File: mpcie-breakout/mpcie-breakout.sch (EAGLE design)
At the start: 36 parts, among them K1 694108106102, U1 IP4234CZ6, U2 LD1085D2T33R, X1 MPCIE-JAE, X2 MINI-USB-SHIELD-UX60-MB-5ST

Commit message: mpcie-breakout: Fix R4 (0603, not 0201 part)
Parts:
- R4: DESCRIPTION RES SMD 1M OHM 5% 1/20W 0201 -> RES SMD 1M OHM 5% 1/10W 0603; LINK http://www.digikey.com/product-detail/en/samsung-electro-me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 -> http://www.digikey.com/product-detail/en/yageo/RC0603JR-071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; MANUFACTURER Samsung Electro-Mechanics America, Inc. -> Yageo; MANUFACTURERPARTNUMBER RC0603J105CS -> RC0603JR-071ML; SOURCEPARTNUMBER 1276-3856-1-ND -> 311-1.0MGRCT-ND
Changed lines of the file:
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@@
 <part name="R4" library="rc-sysmocom" deviceset="RESISTOR" device="_0603" value="1M">
 <attribute name="CLASS" value="RESISTOR"/>
-<attribute name="DESCRIPTION" value="RES SMD 1M OHM 5% 1/20W 0201"/>
-<attribute name="LINK" value="http://www.digikey.com/product-detail/en/samsung-electro-mechanics-america-inc/RC0603J105CS/1276-3856-1-ND/3966828"/>
-<attribute name="MANUFACTURER" value="Samsung Electro-Mechanics America, Inc."/>
-<attribute name="MANUFACTURERPARTNUMBER" value="RC0603J105CS"/>
+<attribute name="DESCRIPTION" value="RES SMD 1M OHM 5% 1/10W 0603"/>
+<attribute name="LINK" value="http://www.digikey.com/product-detail/en/yageo/RC0603JR-071ML/311-1.0MGRCT-ND/729625"/>
+<attribute name="MANUFACTURER" value="Yageo"/>
+<attribute name="MANUFACTURERPARTNUMBER" value="RC0603JR-071ML"/>
 <attribute name="POPULATED" value="TRUE"/>
 <attribute name="ROHSCERTIFICATE" value="UNKNOWN ROHS CERTIFICATE"/>
 <attribute name="SOURCE" value="DIGIKEY"/>
-<attribute name="SOURCEPARTNUMBER" value="1276-3856-1-ND"/>
+<attribute name="SOURCEPARTNUMBER" value="311-1.0MGRCT-ND"/>
 </part>
 <part name="C9" library="rc-sysmocom" deviceset="CAP_CERAMIC" device="_0603" value="100n">
@@
 <instance part="GND11" gate="1" x="30.48" y="96.52"/>
 <instance part="R4" gate="G$1" x="236.22" y="50.8" rot="R90">
+<attribute name="LINK" x="236.22" y="50.8" size="1.778" layer="96" display="off"/>
 <attribute name="DESCRIPTION" x="236.22" y="50.8" size="1.778" layer="96" display="off"/>
 <attribute name="MANUFACTURER" x="236.22" y="50.8" size="1.778" layer="96" display="off"/>
@@
 <attribute name="POPULATED" x="236.22" y="50.8" size="1.778" layer="96" display="off"/>
 <attribute name="CLASS" x="236.22" y="50.8" size="1.778" layer="96" display="off"/>
-<attribute name="LINK" x="236.22" y="50.8" size="1.778" layer="96" display="off"/>
 </instance>
 <instance part="C9" gate="G$1" x="228.6" y="50.8" smashed="yes" rot="R90">

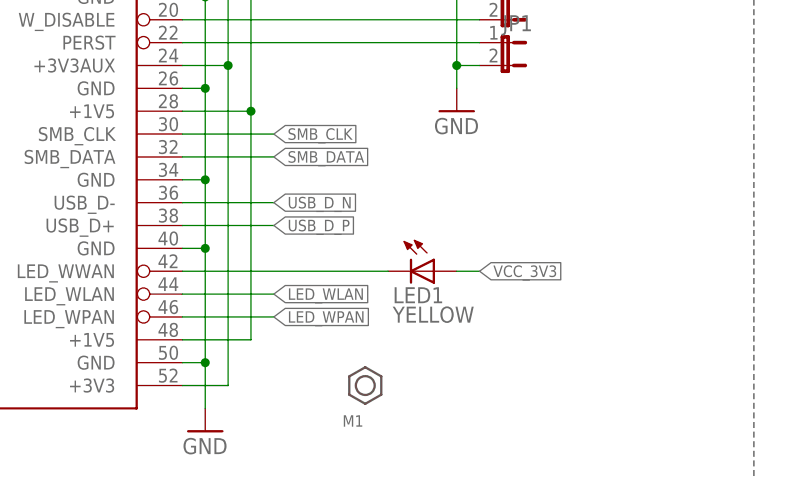
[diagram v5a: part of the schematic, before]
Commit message: mpcie-breakout: Add series LED for LED_WWAN
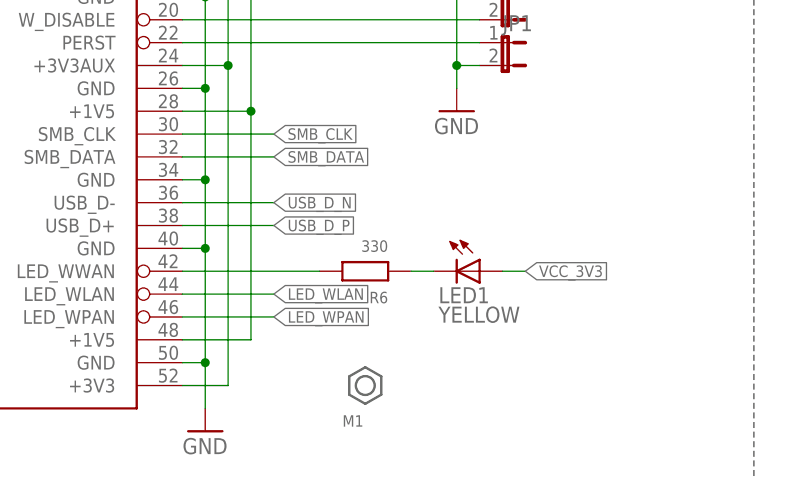
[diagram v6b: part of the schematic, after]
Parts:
- added R6: 330, rc-sysmocom:RESISTOR_0603
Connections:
- new net N$2: LED1.C, R6.1
- net N$3: now also R6.2; no longer LED1.C
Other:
- moved on the sheet: LED1
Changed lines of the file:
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@@
 <schematic xreflabel="%F%N/%S.%C%R" xrefpart="/%S.%C%R">
 <attributes>
-<attribute name="VERSION" value="v1"/>
+<attribute name="VERSION" value="v2"/>
 </attributes>
 <variantdefs>
@@
 <attribute name="SOURCE" value="DIGIKEY"/>
 <attribute name="SOURCEPARTNUMBER" value="490-7217-1-ND"/>
+</part>
+<part name="R6" library="rc-sysmocom" deviceset="RESISTOR" device="_0603" value="330">
+<attribute name="CLASS" value="RESISTOR"/>
+<attribute name="DESCRIPTION" value="RES SMD 330 OHM 5% 1/10W 0603"/>
+<attribute name="LINK" value="http://www.digikey.com/product-detail/en/yageo/RC0603JR-07330RL/311-330GRCT-ND/729716"/>
+<attribute name="MANUFACTURER" value="Yageo"/>
+<attribute name="MANUFACTURERPARTNUMBER" value="RC0603JR-07330RL"/>
+<attribute name="POPULATED" value="TRUE"/>
+<attribute name="ROHSCERTIFICATE" value="UNKNOWN ROHS CERTIFICATE"/>
+<attribute name="SOURCE" value="DIGIKEY"/>
+<attribute name="SOURCEPARTNUMBER" value="311-330GRCT-ND"/>
 </part>
 </parts>
@@
 <attribute name="LINK" x="55.88" y="106.68" size="1.778" layer="96" display="off"/>
 </instance>
-<instance part="LED1" gate="G$1" x="93.98" y="22.86" rot="R270">
-<attribute name="DESCRIPTION" x="93.98" y="22.86" size="1.778" layer="96" display="off"/>
-<attribute name="MANUFACTURER" x="93.98" y="22.86" size="1.778" layer="96" display="off"/>
-<attribute name="MANUFACTURERPARTNUMBER" x="93.98" y="22.86" size="1.778" layer="96" display="off"/>
-<attribute name="SOURCE" x="93.98" y="22.86" size="1.778" layer="96" display="off"/>
-<attribute name="SOURCEPARTNUMBER" x="93.98" y="22.86" size="1.778" layer="96" display="off"/>
-<attribute name="ROHSCERTIFICATE" x="93.98" y="22.86" size="1.778" layer="96" display="off"/>
-<attribute name="POPULATED" x="93.98" y="22.86" size="1.778" layer="96" display="off"/>
-<attribute name="CLASS" x="93.98" y="22.86" size="1.778" layer="96" display="off"/>
-<attribute name="LINK" x="93.98" y="22.86" size="1.778" layer="96" display="off"/>
+<instance part="LED1" gate="G$1" x="99.06" y="22.86" rot="R270">
+<attribute name="DESCRIPTION" x="99.06" y="22.86" size="1.778" layer="96" display="off"/>
+<attribute name="MANUFACTURER" x="99.06" y="22.86" size="1.778" layer="96" display="off"/>
+<attribute name="MANUFACTURERPARTNUMBER" x="99.06" y="22.86" size="1.778" layer="96" display="off"/>
+<attribute name="SOURCE" x="99.06" y="22.86" size="1.778" layer="96" display="off"/>
+<attribute name="SOURCEPARTNUMBER" x="99.06" y="22.86" size="1.778" layer="96" display="off"/>
+<attribute name="ROHSCERTIFICATE" x="99.06" y="22.86" size="1.778" layer="96" display="off"/>
+<attribute name="POPULATED" x="99.06" y="22.86" size="1.778" layer="96" display="off"/>
+<attribute name="CLASS" x="99.06" y="22.86" size="1.778" layer="96" display="off"/>
+<attribute name="LINK" x="99.06" y="22.86" size="1.778" layer="96" display="off"/>
 </instance>
 <instance part="JP1" gate="A" x="101.6" y="48.26" rot="R270">
@@
 <attribute name="POPULATED" x="185.42" y="114.3" size="1.778" layer="96" display="off"/>
 <attribute name="CLASS" x="185.42" y="114.3" size="1.778" layer="96" display="off"/>
+</instance>
+<instance part="R6" gate="G$1" x="86.36" y="22.86" rot="R180">
+<attribute name="DESCRIPTION" x="86.36" y="22.86" size="1.778" layer="96" rot="R90" display="off"/>
+<attribute name="MANUFACTURER" x="86.36" y="22.86" size="1.778" layer="96" rot="R90" display="off"/>
+<attribute name="MANUFACTURERPARTNUMBER" x="86.36" y="22.86" size="1.778" layer="96" rot="R90" display="off"/>
+<attribute name="SOURCE" x="86.36" y="22.86" size="1.778" layer="96" rot="R90" display="off"/>
+<attribute name="SOURCEPARTNUMBER" x="86.36" y="22.86" size="1.778" layer="96" rot="R90" display="off"/>
+<attribute name="ROHSCERTIFICATE" x="86.36" y="22.86" size="1.778" layer="96" rot="R90" display="off"/>
+<attribute name="POPULATED" x="86.36" y="22.86" size="1.778" layer="96" rot="R90" display="off"/>
+<attribute name="CLASS" x="86.36" y="22.86" size="1.778" layer="96" rot="R90" display="off"/>
+<attribute name="LINK" x="86.36" y="22.86" size="1.778" layer="96" rot="R90" display="off"/>
 </instance>
 </instances>
@@
 <segment>
 <pinref part="LED1" gate="G$1" pin="A"/>
-<wire x1="96.52" y1="22.86" x2="99.06" y2="22.86" width="0.1524" layer="91"/>
-<label x="99.06" y="22.86" size="1.27" layer="95" xref="yes"/>
+<wire x1="101.6" y1="22.86" x2="104.14" y2="22.86" width="0.1524" layer="91"/>
+<label x="104.14" y="22.86" size="1.27" layer="95" xref="yes"/>
 </segment>
 <segment>
@@
 <segment>
 <pinref part="X1" gate="G$1" pin="LED_WWAN"/>
-<wire x1="66.04" y1="22.86" x2="88.9" y2="22.86" width="0.1524" layer="91"/>
-<pinref part="LED1" gate="G$1" pin="C"/>
+<wire x1="66.04" y1="22.86" x2="81.28" y2="22.86" width="0.1524" layer="91"/>
+<pinref part="R6" gate="G$1" pin="2"/>
 </segment>
 </net>
@@
 </segment>
 </net>
+<net name="N$2" class="0">
+<segment>
+<pinref part="LED1" gate="G$1" pin="C"/>
+<pinref part="R6" gate="G$1" pin="1"/>
+<wire x1="91.44" y1="22.86" x2="93.98" y2="22.86" width="0.1524" layer="91"/>
+</segment>
+</net>

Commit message: mpcie-breakout: mark C4  as POPULATED=FALSE
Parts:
- C4: POPULATED TRUE -> FALSE
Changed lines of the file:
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@@
 <attribute name="MANUFACTURER" value="UNKNOWN MANUFACTURER"/>
 <attribute name="MANUFACTURERPARTNUMBER" value="UNKNOWN MANUFACTURER PART NUMBER"/>
-<attribute name="POPULATED" value="TRUE"/>
+<attribute name="POPULATED" value="FALSE"/>
 <attribute name="ROHSCERTIFICATE" value="UNKNOWN ROHS CERTIFICATE"/>
 <attribute name="SOURCE" value="UNKNOWN SOURCE"/>

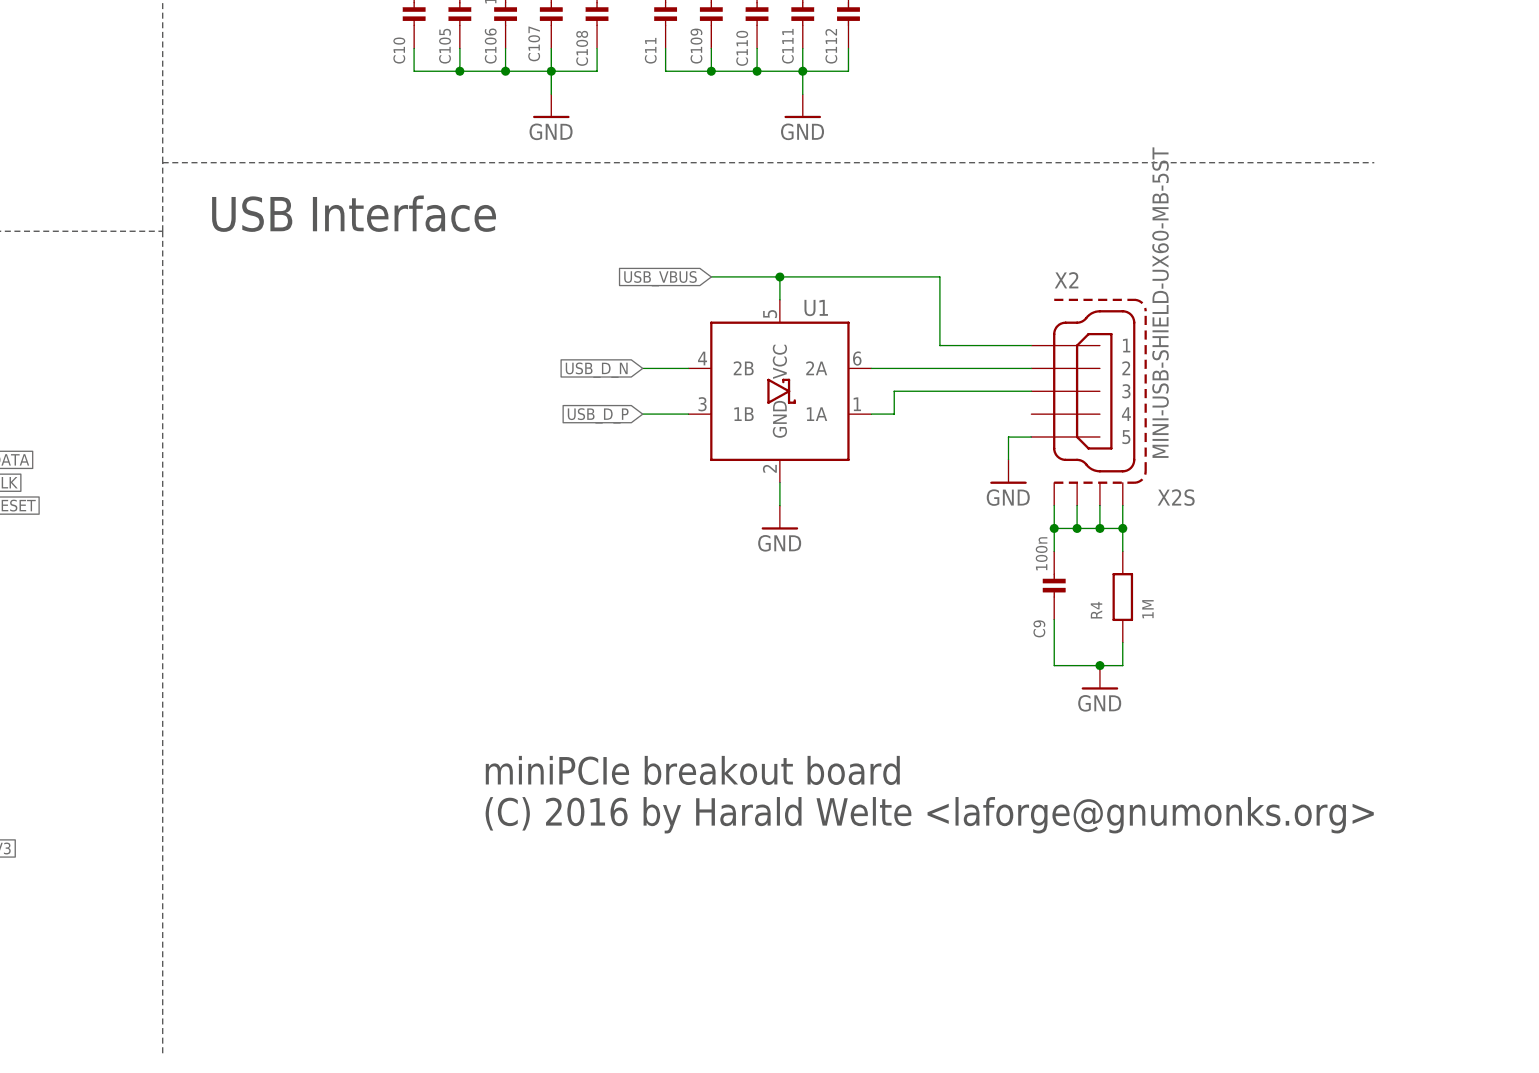
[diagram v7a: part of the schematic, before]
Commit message: mpcie-breakout: Enlarge to 70x70mm, add SMA, U.FL and Mounting Holes
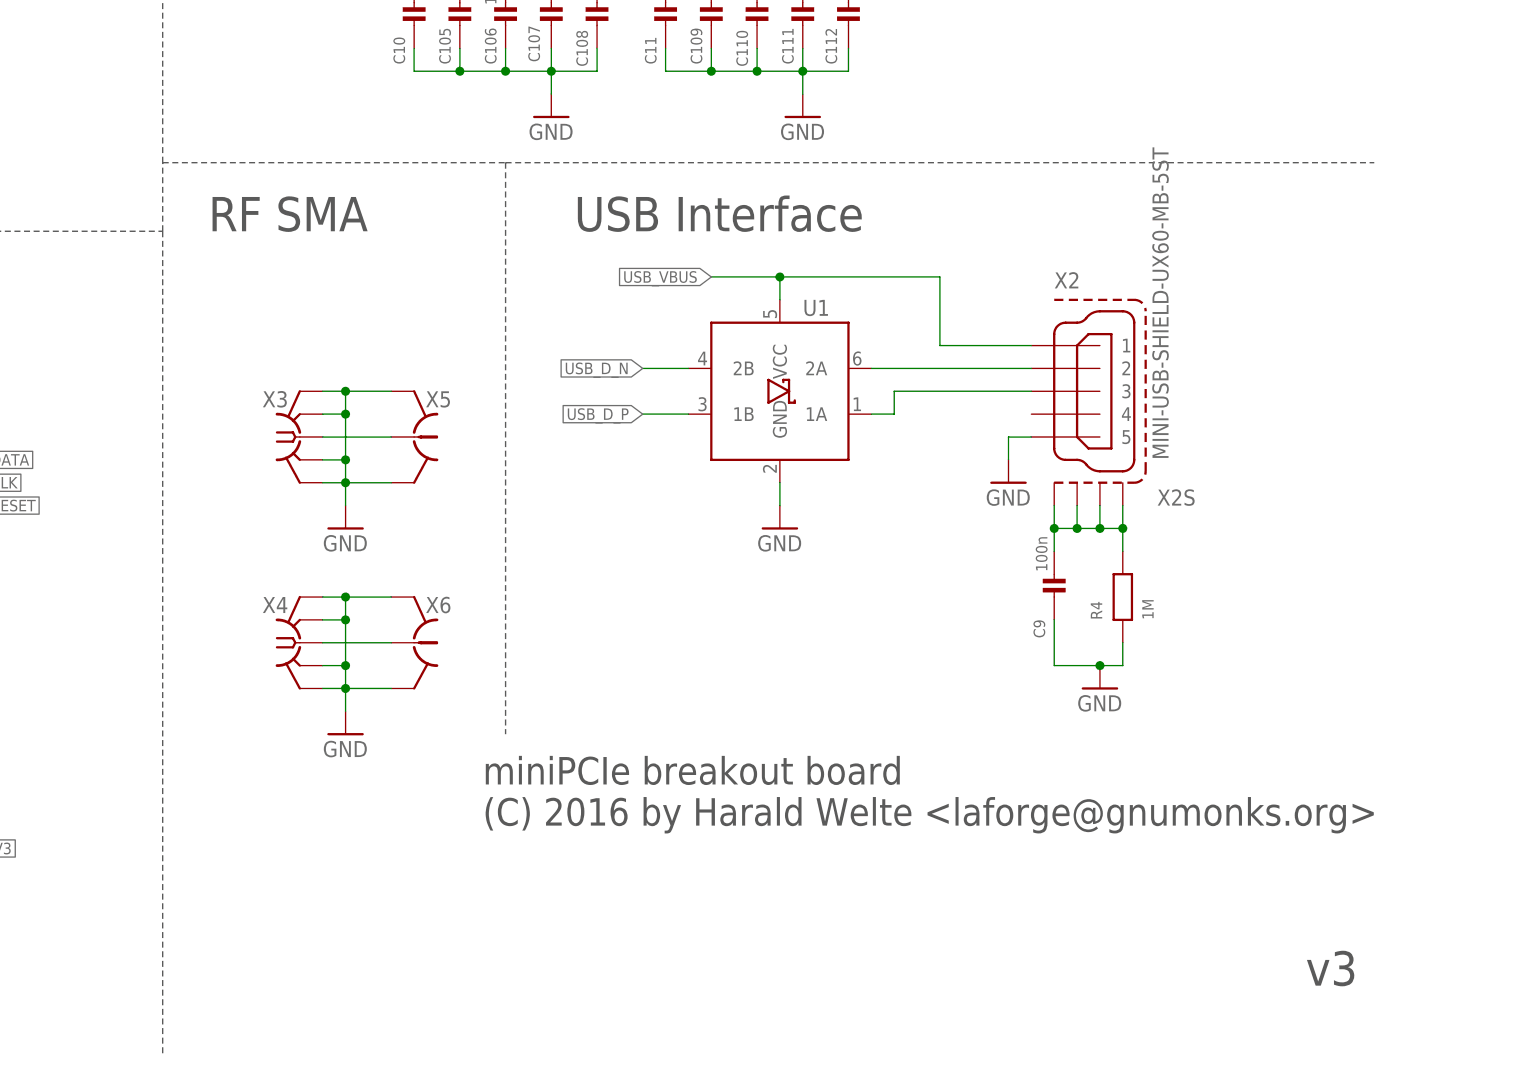
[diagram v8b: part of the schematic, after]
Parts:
- added X3, X4: (no value), laforge:SMA-F-S-TH
- added X5, X6: (no value), laforge:HRS_UFL
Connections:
- new net N$13: X3.1, X5.1
- new net N$14: X4.1, X6.1
- net GND: now also X3.GND@1, X3.GND@2, X3.GND@3, X3.GND@4, X4.GND@1, X4.GND@2, X4.GND@3, X4.GND@4, X5.GND@1, X5.GND@2, X6.GND@1, X6.GND@2
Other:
- note added: "RF SMA"
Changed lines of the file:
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@@
 <schematic xreflabel="%F%N/%S.%C%R" xrefpart="/%S.%C%R">
 <attributes>
-<attribute name="VERSION" value="v2"/>
+<attribute name="VERSION" value="v3"/>
 </attributes>
 <variantdefs>
@@
 </class>
 <class number="1" name="usb" width="0.5" drill="0.15">
+</class>
+<class number="2" name="50 ohm" width="0.9" drill="0">
+<clearance class="2" value="0.152"/>
 </class>
 <class number="3" name="supply" width="0.6" drill="0">
@@
 <attribute name="SOURCEPARTNUMBER" value="311-330GRCT-ND"/>
 </part>
+<part name="X3" library="laforge" deviceset="SMA-F" device="-S-TH"/>
+<part name="X4" library="laforge" deviceset="SMA-F" device="-S-TH"/>
+<part name="X5" library="laforge" deviceset="HRS_UFL" device=""/>
+<part name="X6" library="laforge" deviceset="HRS_UFL" device=""/>
+<part name="GND14" library="supply1" deviceset="GND" device=""/>
+<part name="GND15" library="supply1" deviceset="GND" device=""/>
 </parts>
 <sheets>
@@
 <wire x1="129.54" y1="99.06" x2="129.54" y2="129.54" width="0.1524" layer="97" style="longdash"/>
 <wire x1="129.54" y1="91.44" x2="129.54" y2="0" width="0.1524" layer="97" style="longdash"/>
-<wire x1="129.54" y1="99.06" x2="264.16" y2="99.06" width="0.1524" layer="97" style="longdash"/>
+<wire x1="129.54" y1="99.06" x2="167.64" y2="99.06" width="0.1524" layer="97" style="longdash"/>
+<wire x1="167.64" y1="99.06" x2="264.16" y2="99.06" width="0.1524" layer="97" style="longdash"/>
 <wire x1="129.54" y1="134.62" x2="264.16" y2="134.62" width="0.1524" layer="97" style="longdash"/>
 <wire x1="264.16" y1="134.62" x2="264.16" y2="137.16" width="0.1524" layer="97" style="longdash"/>
@@
 <text x="134.62" y="172.72" size="3.81" layer="97" font="vector" ratio="12">Power Supply</text>
 <text x="132.08" y="127" size="3.81" layer="97" font="vector" ratio="12">Blocking Capacitors</text>
-<text x="134.62" y="91.44" size="3.81" layer="97" font="vector" ratio="12">USB Interface</text>
+<text x="175.26" y="91.44" size="3.81" layer="97" font="vector" ratio="12">USB Interface</text>
 <text x="132.08" y="137.16" size="2.54" layer="97" font="vector" ratio="12">JP3 1-2: USB bus powered
 JP3 2-3: external 5V supply</text>
+<text x="134.62" y="91.44" size="3.81" layer="97" font="vector" ratio="12">RF SMA</text>
+<wire x1="167.64" y1="99.06" x2="167.64" y2="35.56" width="0.1524" layer="97" style="longdash"/>
+<text x="256.54" y="7.62" size="3.81" layer="97">&gt;VERSION</text>
 </plain>
 <instances>
@@
 <attribute name="LINK" x="86.36" y="22.86" size="1.778" layer="96" rot="R90" display="off"/>
 </instance>
+<instance part="X3" gate="G" x="144.78" y="68.58"/>
+<instance part="X4" gate="G" x="144.78" y="45.72"/>
+<instance part="X5" gate="G$1" x="157.48" y="68.58" rot="MR0"/>
+<instance part="X6" gate="G$1" x="157.48" y="45.72" rot="MR0"/>
+<instance part="GND14" gate="1" x="149.86" y="58.42"/>
+<instance part="GND15" gate="1" x="149.86" y="35.56"/>
 </instances>
 <busses>
@@
 <pinref part="R5" gate="G$1" pin="1"/>
 <pinref part="GND13" gate="1" pin="GND"/>
+</segment>
+<segment>
+<pinref part="X3" gate="G" pin="GND@1"/>
+<pinref part="X5" gate="G$1" pin="GND@1"/>
+<wire x1="147.32" y1="73.66" x2="149.86" y2="73.66" width="0.1524" layer="91"/>
+<pinref part="X3" gate="G" pin="GND@2"/>
+<wire x1="149.86" y1="73.66" x2="154.94" y2="73.66" width="0.1524" layer="91"/>
+<wire x1="147.32" y1="71.12" x2="149.86" y2="71.12" width="0.1524" layer="91"/>
+<wire x1="149.86" y1="71.12" x2="149.86" y2="73.66" width="0.1524" layer="91"/>
+<wire x1="149.86" y1="71.12" x2="149.86" y2="66.04" width="0.1524" layer="91"/>
+<pinref part="X3" gate="G" pin="GND@3"/>
+<wire x1="149.86" y1="66.04" x2="147.32" y2="66.04" width="0.1524" layer="91"/>
+<wire x1="149.86" y1="66.04" x2="149.86" y2="63.5" width="0.1524" layer="91"/>
+<pinref part="X3" gate="G" pin="GND@4"/>
+<wire x1="149.86" y1="63.5" x2="149.86" y2="60.96" width="0.1524" layer="91"/>
+<wire x1="147.32" y1="63.5" x2="149.86" y2="63.5" width="0.1524" layer="91"/>
+<pinref part="X5" gate="G$1" pin="GND@2"/>
+<wire x1="149.86" y1="63.5" x2="154.94" y2="63.5" width="0.1524" layer="91"/>
+<junction x="149.86" y="66.04"/>
+<junction x="149.86" y="71.12"/>
+<junction x="149.86" y="73.66"/>
+<junction x="149.86" y="63.5"/>
+<pinref part="GND14" gate="1" pin="GND"/>
+</segment>
+<segment>
+<pinref part="X4" gate="G" pin="GND@1"/>
+<pinref part="X6" gate="G$1" pin="GND@1"/>
+<wire x1="147.32" y1="50.8" x2="149.86" y2="50.8" width="0.1524" layer="91"/>
+<pinref part="X4" gate="G" pin="GND@2"/>
+<wire x1="149.86" y1="50.8" x2="154.94" y2="50.8" width="0.1524" layer="91"/>
+<wire x1="147.32" y1="48.26" x2="149.86" y2="48.26" width="0.1524" layer="91"/>
+<wire x1="149.86" y1="48.26" x2="149.86" y2="50.8" width="0.1524" layer="91"/>
+<wire x1="149.86" y1="48.26" x2="149.86" y2="43.18" width="0.1524" layer="91"/>
+<pinref part="X4" gate="G" pin="GND@3"/>
+<wire x1="149.86" y1="43.18" x2="149.86" y2="40.64" width="0.1524" layer="91"/>
+<wire x1="149.86" y1="40.64" x2="149.86" y2="38.1" width="0.1524" layer="91"/>
+<wire x1="147.32" y1="43.18" x2="149.86" y2="43.18" width="0.1524" layer="91"/>
+<pinref part="X4" gate="G" pin="GND@4"/>
+<wire x1="147.32" y1="40.64" x2="149.86" y2="40.64" width="0.1524" layer="91"/>
+<pinref part="X6" gate="G$1" pin="GND@2"/>
+<wire x1="154.94" y1="40.64" x2="149.86" y2="40.64" width="0.1524" layer="91"/>
+<junction x="149.86" y="50.8"/>
+<junction x="149.86" y="48.26"/>
+<junction x="149.86" y="43.18"/>
+<junction x="149.86" y="40.64"/>
+<pinref part="GND15" gate="1" pin="GND"/>
 </segment>
 </net>
@@
 </segment>
 </net>
+<net name="N$13" class="2">
+<segment>
+<pinref part="X3" gate="G" pin="1"/>
+<pinref part="X5" gate="G$1" pin="1"/>
+<wire x1="147.32" y1="68.58" x2="154.94" y2="68.58" width="0.1524" layer="91"/>
+</segment>
+</net>
+<net name="N$14" class="2">
+<segment>
+<pinref part="X4" gate="G" pin="1"/>
+<pinref part="X6" gate="G$1" pin="1"/>
+<wire x1="147.32" y1="45.72" x2="154.94" y2="45.72" width="0.1524" layer="91"/>
+</segment>
+</net>
